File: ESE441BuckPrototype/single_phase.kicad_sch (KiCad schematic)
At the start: 11 parts

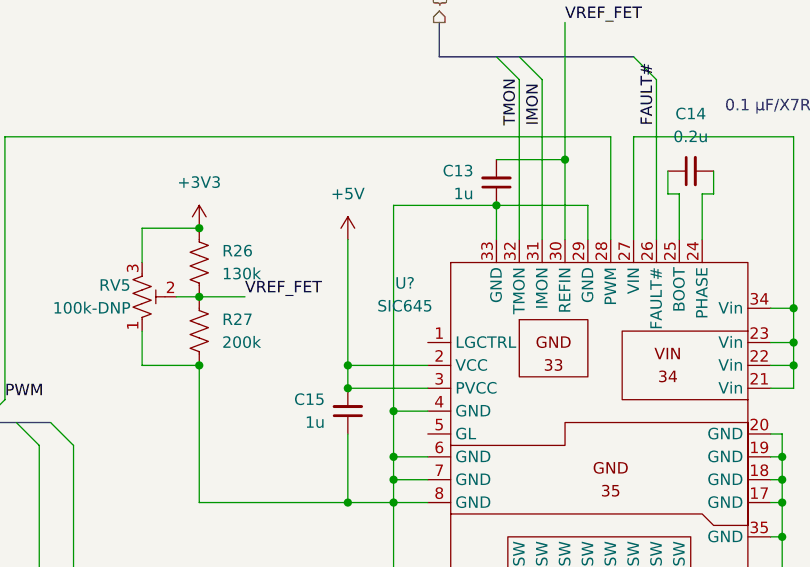
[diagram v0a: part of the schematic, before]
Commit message: Add optional LDO and annotations
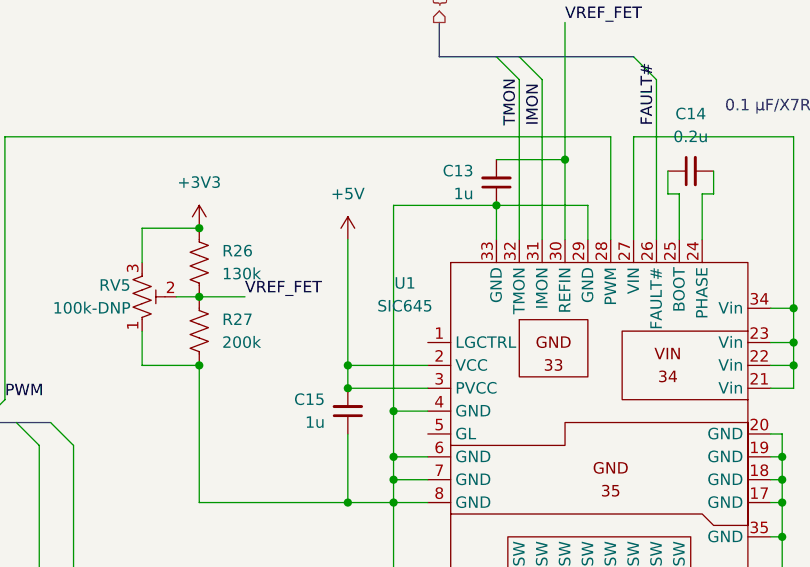
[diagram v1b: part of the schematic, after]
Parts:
- gave numbers to parts that had none: 1
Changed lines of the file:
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@@
   (symbol (lib_id "power:GND") (at 101.6 95.25 0) (unit 1)
     (in_bom yes) (on_board yes) (fields_autoplaced)
-    (property "Reference" "#PWR?" (id 0) (at 101.6 101.6 0)
+    (property "Reference" "#PWR0124" (id 0) (at 101.6 101.6 0)
       (effects (font (size 1.27 1.27)) hide)
     )
@@
   (symbol (lib_id "power:+3V3") (at 80.01 45.72 0) (unit 1)
     (in_bom yes) (on_board yes) (fields_autoplaced)
-    (property "Reference" "#PWR?" (id 0) (at 80.01 49.53 0)
+    (property "Reference" "#PWR0125" (id 0) (at 80.01 49.53 0)
       (effects (font (size 1.27 1.27)) hide)
     )
@@
   (symbol (lib_id "power:+5V") (at 96.52 46.99 0) (unit 1)
     (in_bom yes) (on_board yes) (fields_autoplaced)
-    (property "Reference" "#PWR?" (id 0) (at 96.52 50.8 0)
+    (property "Reference" "#PWR0121" (id 0) (at 96.52 50.8 0)
       (effects (font (size 1.27 1.27)) hide)
     )
@@
   (symbol (lib_id "power:+1V0") (at 205.74 59.69 0) (unit 1)
     (in_bom yes) (on_board yes) (fields_autoplaced)
-    (property "Reference" "#PWR?" (id 0) (at 205.74 63.5 0)
+    (property "Reference" "#PWR0123" (id 0) (at 205.74 63.5 0)
       (effects (font (size 1.27 1.27)) hide)
     )
@@
   (symbol (lib_id "CustomPartsLibrary:SIC645") (at 124.46 67.31 0) (unit 1)
     (in_bom yes) (on_board yes) (fields_autoplaced)
-    (property "Reference" "U?" (id 0) (at 102.87 51.8412 0))
+    (property "Reference" "U1" (id 0) (at 102.87 51.8412 0))
     (property "Value" "SIC645" (id 1) (at 102.87 54.3812 0))
     (property "Footprint" "" (id 2) (at 119.38 59.69 0)
@@
   (symbol (lib_id "power:GNDPWR") (at 205.74 83.82 0) (unit 1)
     (in_bom yes) (on_board yes) (fields_autoplaced)
-    (property "Reference" "#PWR?" (id 0) (at 205.74 88.9 0)
-      (effects (font (size 1.27 1.27)) hide)
-    )
+    (property "Reference" "#PWR0122" (id 0) (at 205.74 88.9 0)
+      (effects (font (size 1.27 1.27)) hide)
+    )

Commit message: Connect enable to MCU; Testpoints
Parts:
- added TP6: TestPoint, symbol Connector:TestPoint
- added TP7, TP8: TestPoint, TestPoint:TestPoint_Loop_D2.50mm_Drill1.0mm_LowProfile, symbol Connector:TestPoint
- C14: Requirements (none) -> 0.1 μF/X7R to 0.22 μF/X7R
- L1: value L -> 4.7u
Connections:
- net +1V0: now also TP8.1
- net ISP: now also TP7.1
- net at L1.1, R25.1, U1.10 (SW)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: now also TP6.1
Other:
- note removed: "0.1 μF/X7R to 0.22 μF/X7R"
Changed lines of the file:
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@@
   (junction (at 195.58 72.39) (diameter 0) (color 0 0 0 0)
   )
+  (junction (at 165.1 64.77) (diameter 0) (color 0 0 0 0)
+  )
   (junction (at 96.52 60.96) (diameter 0) (color 0 0 0 0)
   )
@@
   (wire (pts (xy 146.05 60.96) (xy 146.05 63.5))
     (stroke (width 0) (type default) (color 0 0 0 0))
-  )
-  (text "0.1 μF/X7R to 0.22 μF/X7R" (at 138.43 33.02 0)
-    (effects (font (size 1.27 1.27)) (justify left bottom))
   )
   (label "VREF_FET" (at 120.65 22.86 0)
@@
     (in_bom yes) (on_board yes) (fields_autoplaced)
     (property "Reference" "L1" (id 0) (at 179.07 58.42 90))
-    (property "Value" "L" (id 1) (at 179.07 60.96 90))
+    (property "Value" "4.7u" (id 1) (at 179.07 60.96 90))
     (property "Footprint" "Inductor_SMD:L_7.3x7.3_H4.5" (id 2) (at 179.07 64.77 0)
       (effects (font (size 1.27 1.27)) hide)
@@
       (effects (font (size 1.27 1.27)) hide)
     )
+    (property "Requirements" "0.1 μF/X7R to 0.22 μF/X7R" (id 4) (at 152.4 34.29 90))
     (pin "1")
     (pin "2")
@@
     (pin "1")
     (pin "2")
+  )
+  (symbol (lib_id "Connector:TestPoint") (at 180.34 72.39 0) (unit 1)
+    (in_bom yes) (on_board yes)
+    (property "Reference" "TP7" (id 0) (at 179.07 67.8179 0)
+      (effects (font (size 1.27 1.27)) (justify left))
+    )
+    (property "Value" "TestPoint" (id 1) (at 182.88 70.3579 0)
+      (effects (font (size 1.27 1.27)) (justify left) hide)
+    )
+    (property "Footprint" "TestPoint:TestPoint_Loop_D2.50mm_Drill1.0mm_LowProfile" (id 2) (at 185.42 72.39 0)
+      (effects (font (size 1.27 1.27)) hide)
+    )
+    (property "Datasheet" "~" (id 3) (at 185.42 72.39 0)
+      (effects (font (size 1.27 1.27)) hide)
+    )
+    (pin "1")
   )
   (symbol (lib_id "power:+5V") (at 96.52 46.99 0) (unit 1)
@@
     (pin "1")
   )
+  (symbol (lib_id "Connector:TestPoint") (at 195.58 64.77 0) (unit 1)
+    (in_bom yes) (on_board yes) (fields_autoplaced)
+    (property "Reference" "TP8" (id 0) (at 198.12 61.4679 0)
+      (effects (font (size 1.27 1.27)) (justify left))
+    )
+    (property "Value" "TestPoint" (id 1) (at 198.12 62.7379 0)
+      (effects (font (size 1.27 1.27)) (justify left) hide)
+    )
+    (property "Footprint" "TestPoint:TestPoint_Loop_D2.50mm_Drill1.0mm_LowProfile" (id 2) (at 200.66 64.77 0)
+      (effects (font (size 1.27 1.27)) hide)
+    )
+    (property "Datasheet" "~" (id 3) (at 200.66 64.77 0)
+      (effects (font (size 1.27 1.27)) hide)
+    )
+    (pin "1")
+  )
   (symbol (lib_id "Device:C_Small") (at 113.03 40.64 0) (mirror x) (unit 1)
     (in_bom yes) (on_board yes) (fields_autoplaced)
@@
     (pin "2")
   )
+  (symbol (lib_id "Connector:TestPoint") (at 165.1 64.77 0) (unit 1)
+    (in_bom yes) (on_board yes) (fields_autoplaced)
+    (property "Reference" "TP6" (id 0) (at 167.64 61.4679 0)
+      (effects (font (size 1.27 1.27)) (justify left))
+    )
+    (property "Value" "TestPoint" (id 1) (at 167.64 62.7379 0)
+      (effects (font (size 1.27 1.27)) (justify left) hide)
+    )
+    (property "Footprint" "" (id 2) (at 170.18 64.77 0)
+      (effects (font (size 1.27 1.27)) hide)
+    )
+    (property "Datasheet" "~" (id 3) (at 170.18 64.77 0)
+      (effects (font (size 1.27 1.27)) hide)
+    )
+    (pin "1")
+  )
   (symbol (lib_id "Device:C_Small") (at 96.52 66.04 0) (mirror x) (unit 1)
